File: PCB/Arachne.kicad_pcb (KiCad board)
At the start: 2 copper layers, 100 x 75 mm, 275 parts, among them J201 SW2, J301 SW2, J401 SW2, J501 SW2, J601 SW2, J701 SW2, J801 V_IN, J901 USB_B, J902 PROG_CONN_STM_6p, J903 DBG_UART, M201 Stepper_Motor_bipolar, M301 Stepper_Motor_bipolar, M401 Stepper_Motor_bipolar, M501 Stepper_Motor_bipolar, M601 Stepper_Motor_bipolar, M701 Stepper_Motor_bipolar, Q801 AOD4189, SW101 SW_Push, U101 STM32L452CEUx, U102 WS2818B, U201 L6470_HTSSOP28, U301 L6470_HTSSOP28, U401 L6470_HTSSOP28, U501 L6470_HTSSOP28, U601 L6470_HTSSOP28, U701 L6470_HTSSOP28, U801 ACS712xLCTR-20A, U802 NCP1117-5.0_SOT223, U803 L5973D, U804 NCP1117-3.3_SOT223, U901 USBLC6-2SC6

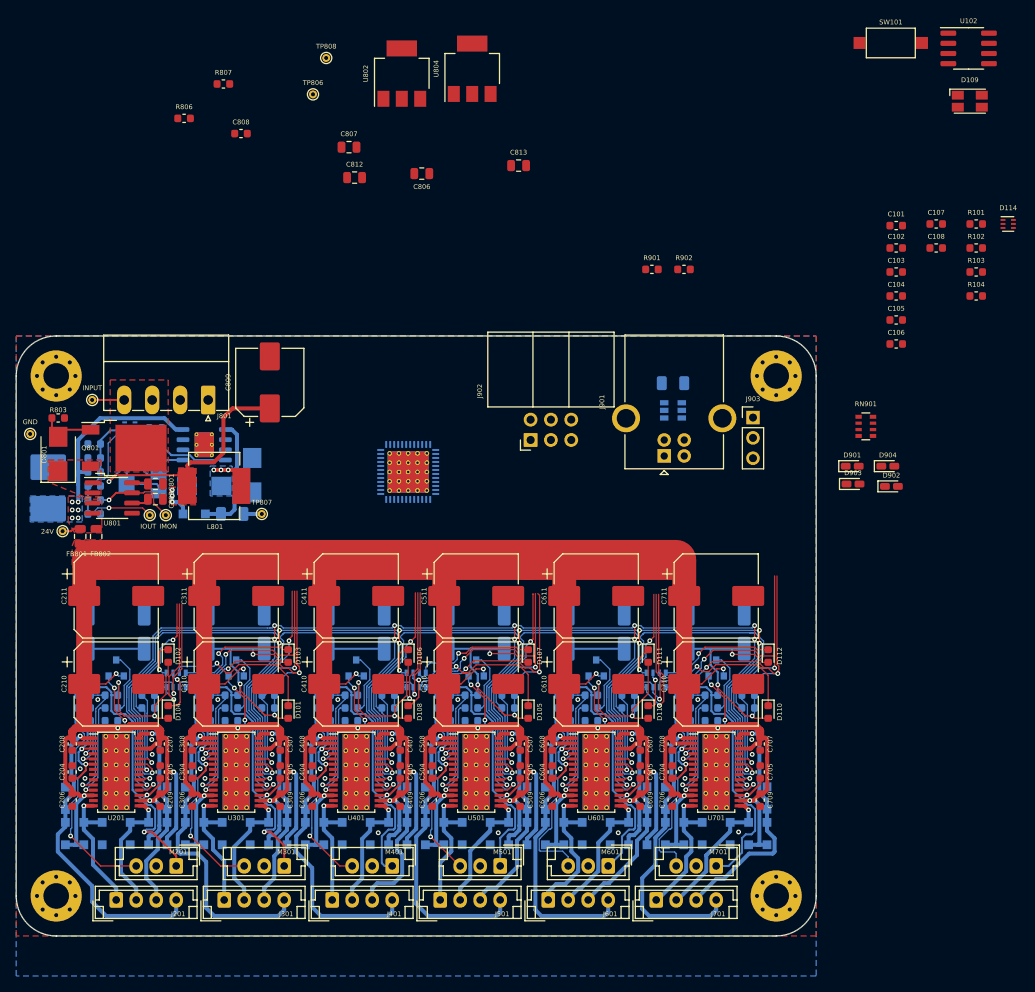
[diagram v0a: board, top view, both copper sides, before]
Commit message: PCB: create new layout for power supply, route LED signalization and reset
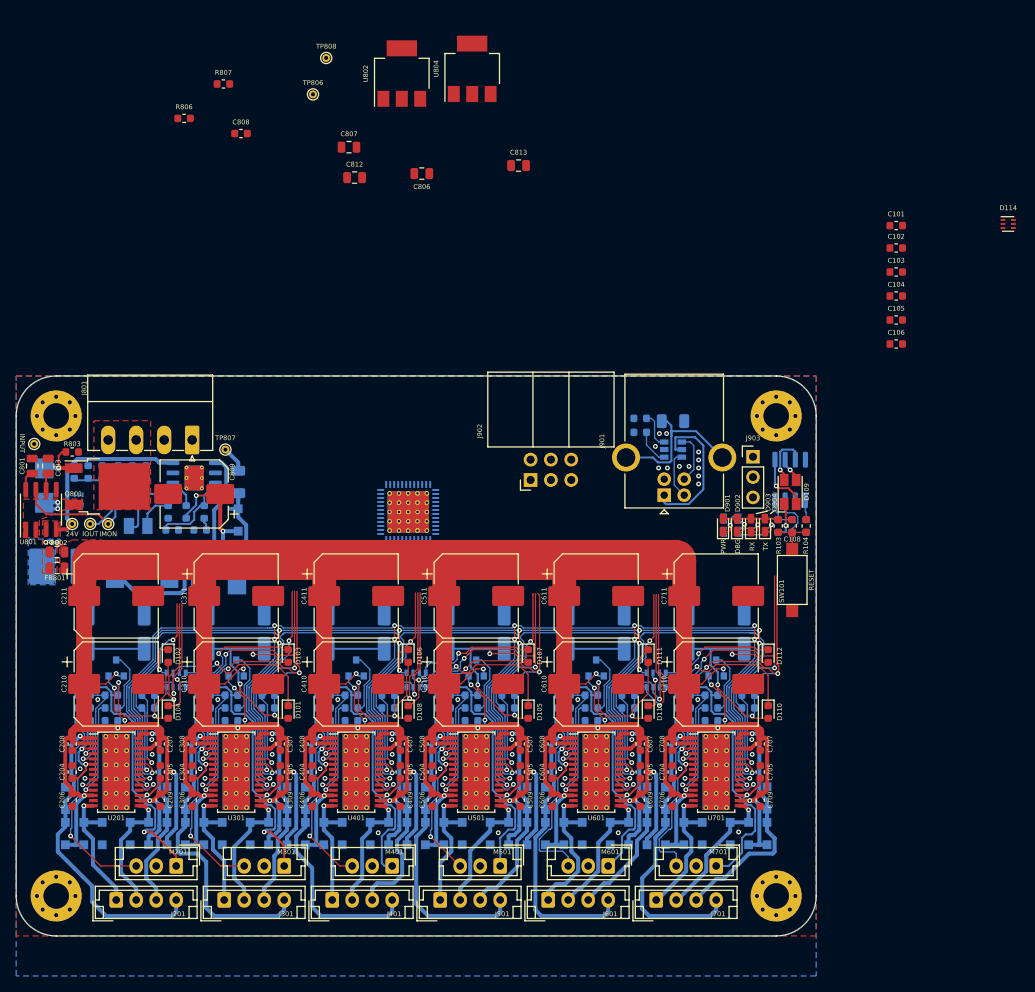
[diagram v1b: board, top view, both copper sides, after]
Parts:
- removed TP802: GND, TestPoint:TestPoint_THTPad_D1.0mm_Drill0.5mm
- C107, D801, L801, R101, R102, R901, R902, RN901, U102: moved to B.Cu
- moved SW101 68.2 mm to (197.0, 105.5), turned to 270 degrees
- moved U102 58.4 mm to (196.8, 93.0), turned to 270 degrees
- moved D109 53.8 mm to (196.8, 94.5), turned to 90 degrees
- moved R101 45.1 mm to (195.2, 98.8), turned to 90 degrees
- moved C107 41.8 mm to (197.0, 98.8), turned to 270 degrees
- moved R102 40.7 mm to (198.8, 98.8), turned to 270 degrees
- moved R103 40.3 mm to (195.2, 98.8), turned to 270 degrees
- moved C108 39.1 mm to (197.0, 98.8), turned to 90 degrees
- moved R104 35.8 mm to (198.8, 98.8), turned to 90 degrees
- moved R902 21.1 mm to (178.0, 87.0)
- moved RN901 20.9 mm to (189.3, 98.7), turned to 180 degrees
- moved D902 19.9 mm to (190.1, 98.7), turned to 90 degrees
- moved R901 18.7 mm to (178.0, 85.3)
- moved D901 17.8 mm to (188.3, 98.7), turned to 90 degrees
- moved D904 17.0 mm to (193.6, 98.7), turned to 90 degrees
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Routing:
- net Net-(J901-Pad5): track 0.00 -> 20.1 mm
- net USB_VCC: track 2.30 -> 21.7 mm
- net /I_MON: track 23.0 -> 13.1 mm, vias 1 -> 0
- net Net-(D805-Pad1): track 12.1 -> 20.6 mm, vias 3 -> 0
- net Net-(R802-Pad1): track 11.1 -> 19.1 mm, vias 1 -> 0
- net Net-(D109-Pad4): track 0.00 -> 7.37 mm, vias 0 -> 1
- net +3V3: track 510.9 -> 517.8 mm
- net Net-(D109-Pad2): track 0.00 -> 6.83 mm, vias 0 -> 1
- net /Interface/USB+: track 0.00 -> 6.38 mm
- net Net-(D904-Pad1): track 0.00 -> 6.24 mm, vias 0 -> 1
- net /Interface/USB-: track 0.00 -> 6.07 mm
- net Net-(C108-Pad1): track 0.00 -> 5.56 mm
- net Net-(C107-Pad2): track 0.00 -> 5.43 mm
- net Net-(C107-Pad1): track 0.00 -> 5.15 mm
- net +5V: track 2.05 -> 7.03 mm, vias 0 -> 1
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- removed copper zone on F.Cu, net Net-(C809-Pad1)
- removed copper zone on B.Cu, net Net-(D805-Pad1)
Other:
- board size 100 x 75 mm -> 100 x 70 mm
- board text added: "DBG"
- board text added: "PWR"
- board text added: "RESET"
- board text added: "RX"
- board text added: "TX"
- board text removed: "GND"

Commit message: PCB: routing of linear regulators, enhance ground connection (power supply)
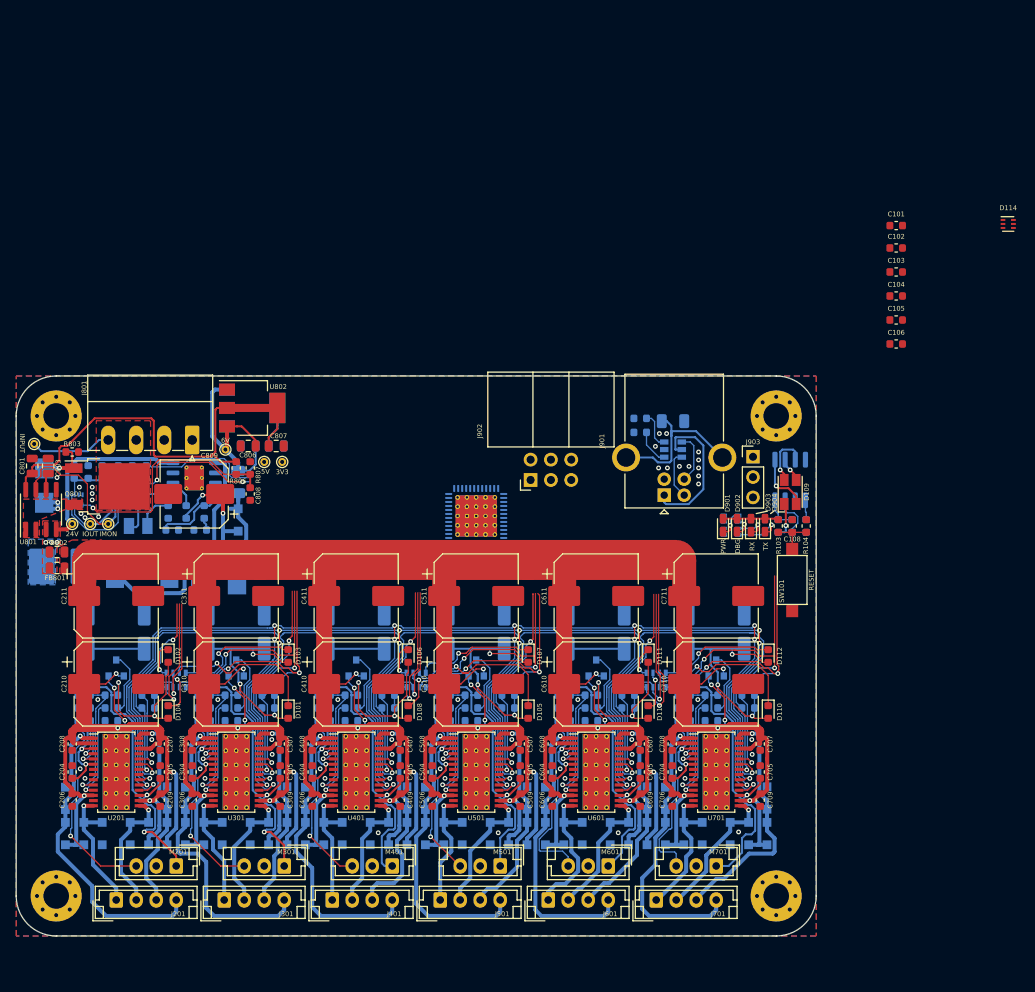
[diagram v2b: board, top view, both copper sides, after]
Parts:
- C812, C813, U804: moved to B.Cu
- moved TP808 50.8 mm to (133.2, 90.8)
- moved U804 50.5 mm to (129.5, 84.0), turned to 0 degrees
- moved R807 48.1 mm to (129.2, 91.5), turned to 90 degrees
- moved TP806 46.4 mm to (131.0, 90.8)
- moved C813 46.3 mm to (132.5, 88.8)
- moved U802 45.8 mm to (129.5, 84.0), turned to 0 degrees
- moved C808 45.1 mm to (129.2, 94.8), turned to 270 degrees
- moved R806 44.2 mm to (127.5, 91.5), turned to 270 degrees
- moved C806 40.4 mm to (129.0, 88.8)
- moved C807 38.4 mm to (132.5, 88.8)
- moved C812 36.1 mm to (129.0, 88.8), turned to 180 degrees
- moved U101 8.51 mm to (157.5, 97.5)
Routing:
- net +5V: track 7.03 -> 60.9 mm
- net /PWR_MON: track 3.50 -> 39.0 mm, vias 0 -> 2
- net /5V_MON: track 0.00 -> 29.6 mm, vias 0 -> 1
- net USB_VCC: track 21.7 -> 44.3 mm
- net /I_MON: track 13.1 -> 32.1 mm
- net +3V3: track 517.8 -> 529.3 mm
- net Net-(J801-Pad3): track 0.00 -> 10.2 mm
- net Net-(R802-Pad1): track 19.1 -> 23.5 mm
- net GND: vias 46 -> 54
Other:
- board text added: "3V3"
- board text added: "5V"
- board text added: "6V"

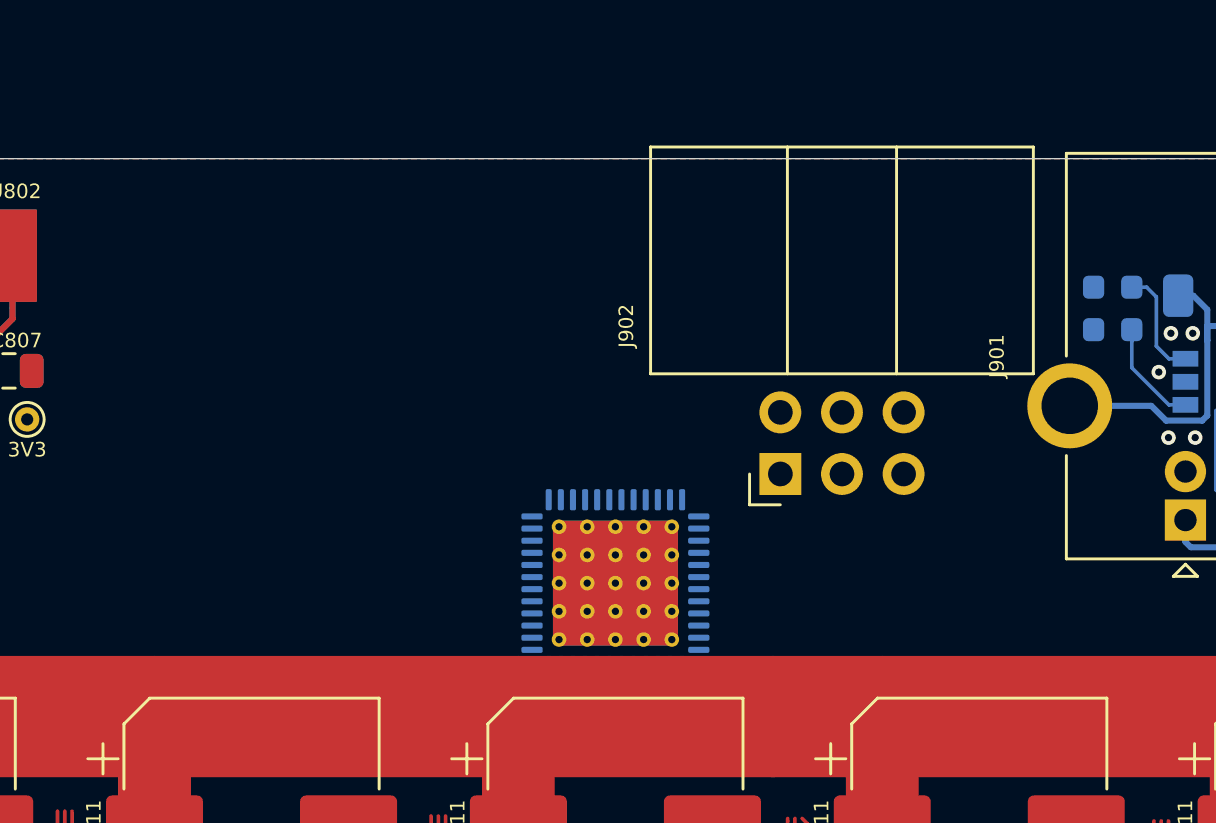
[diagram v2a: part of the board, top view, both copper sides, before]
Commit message: PCB: change programing and debugging IDC connectors to vertical version
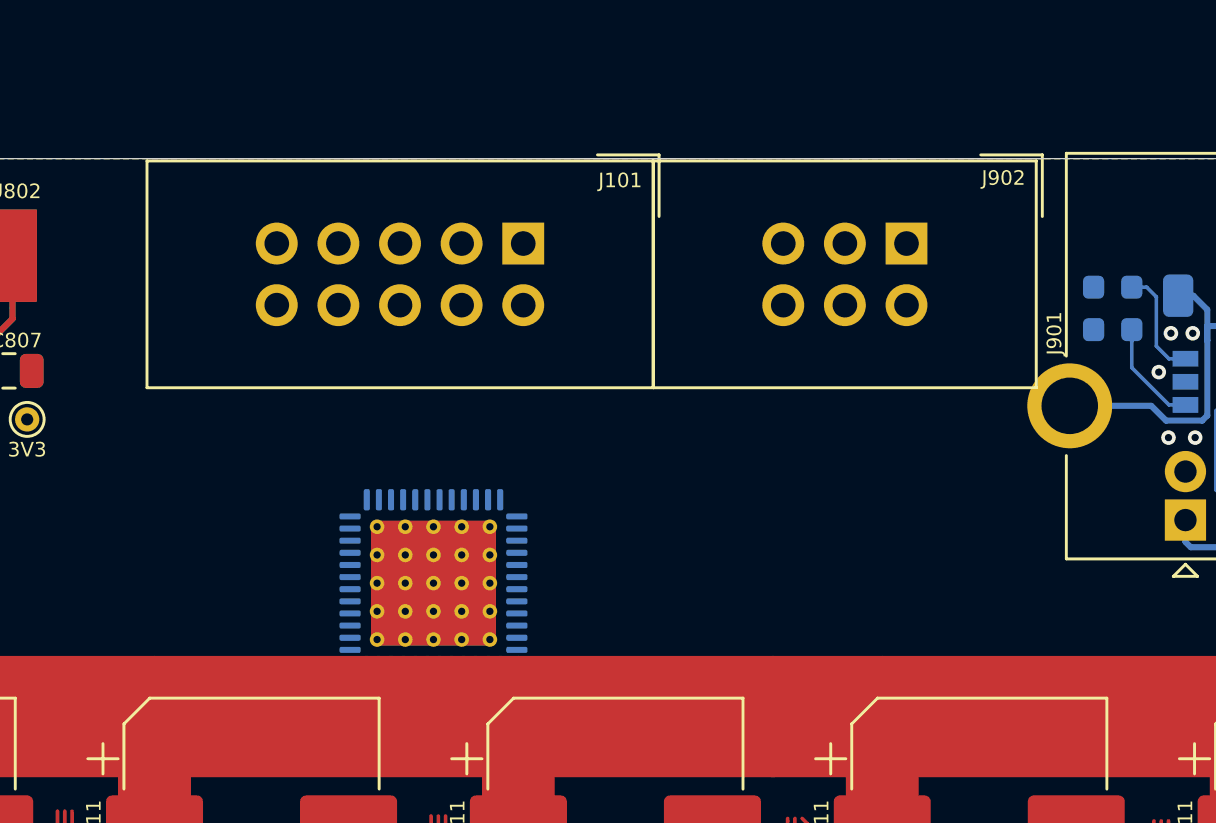
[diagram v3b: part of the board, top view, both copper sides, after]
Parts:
- added J101: Salae_logic, Connector_IDC:IDC-Header_2x05_P2.54mm_Vertical, F.Cu at (153.7, 83.5)
- J902: footprint Connector_IDC:IDC-Header_2x03_P2.54mm_Horizontal -> Connector_IDC:IDC-Header_2x03_P2.54mm_Vertical
- moved J902 10.8 mm to (169.5, 83.5), turned to 270 degrees
- moved U101 7.50 mm to (150.0, 97.5)
